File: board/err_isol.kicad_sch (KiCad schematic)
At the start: 5 parts, among them U16 H11L1

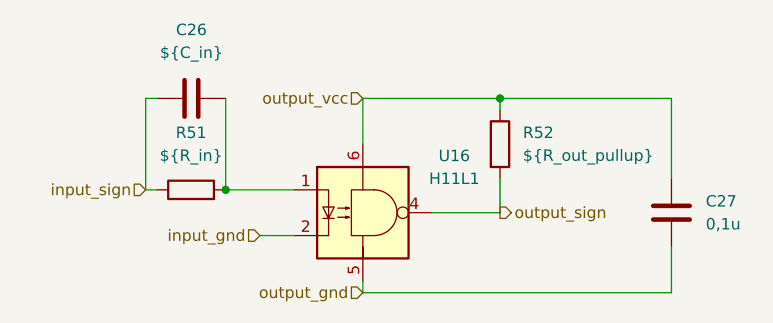
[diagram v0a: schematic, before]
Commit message: Finalização da placa, trilhas, planos de terra e footprint TJA1050
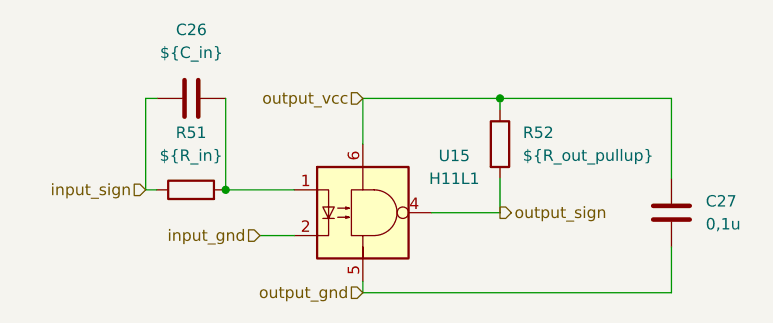
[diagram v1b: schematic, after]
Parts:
- renumbered U16 to U15
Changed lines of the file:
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@@
 		(dnp no)
 		(fields_autoplaced yes)
-		(property "Reference" "U16"
+		(property "Reference" "U15"
 			(at 113.03 83.8514 0)
 			(effects
@@
 			(project "board"
 				(path "/d7be55ed-3561-4de6-aa99-76e883d44fb9/90c49c41-4e5e-4cb7-8d94-45cf3dbd4784/89eae5c2-3bab-4caa-9966-8abf6d8721dc/80c37905-981e-40ed-8bc4-c6bd1141d6f2"
-					(reference "U16")
+					(reference "U15")
 					(unit 1)
 				)
 				(path "/d7be55ed-3561-4de6-aa99-76e883d44fb9/90c49c41-4e5e-4cb7-8d94-45cf3dbd4784/8e1b14a0-5a44-45bc-9dce-fdb022fd1001/80c37905-981e-40ed-8bc4-c6bd1141d6f2"
-					(reference "U19")
+					(reference "U21")
 					(unit 1)
 				)
 				(path "/d7be55ed-3561-4de6-aa99-76e883d44fb9/90c49c41-4e5e-4cb7-8d94-45cf3dbd4784/f0530d57-4207-4b28-8d03-9cc33be1a412/80c37905-981e-40ed-8bc4-c6bd1141d6f2"
-					(reference "U12")
+					(reference "U11")
 					(unit 1)
 				)

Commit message: Criação da placa de alimentação
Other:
- company: (none) -> Escola Politécnica da Universidade de São Paulo
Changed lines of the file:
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@@
 	(generator_version "8.0")
 	(paper "A4")
+	(title_block
+		(date "2025-10-02")
+		(company "Escola Politécnica da Universidade de São Paulo")
+	)
 	(junction
 		(at 87.63 87.63)
@@
 				)
 				(path "/d7be55ed-3561-4de6-aa99-76e883d44fb9/90c49c41-4e5e-4cb7-8d94-45cf3dbd4784/8e1b14a0-5a44-45bc-9dce-fdb022fd1001/80c37905-981e-40ed-8bc4-c6bd1141d6f2"
-					(reference "C32")
+					(reference "C35")
 					(unit 1)
 				)
@@
 				)
 				(path "/d7be55ed-3561-4de6-aa99-76e883d44fb9/90c49c41-4e5e-4cb7-8d94-45cf3dbd4784/8e1b14a0-5a44-45bc-9dce-fdb022fd1001/80c37905-981e-40ed-8bc4-c6bd1141d6f2"
-					(reference "C31")
-					(unit 1)
-				)
+					(reference "C34")
+					(unit 1)
+				)
